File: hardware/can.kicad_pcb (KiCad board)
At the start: 2 copper layers, 45 x 35 mm, 33 parts, among them J1 DB9, P1 CON-SENSOR, P2 CONN_5, P3 CONN_5, U1 M24C64, U2 SC16IS740, U3 SP3232EBCN, U4 DRILL, U5 DRILL, U6 DRILL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

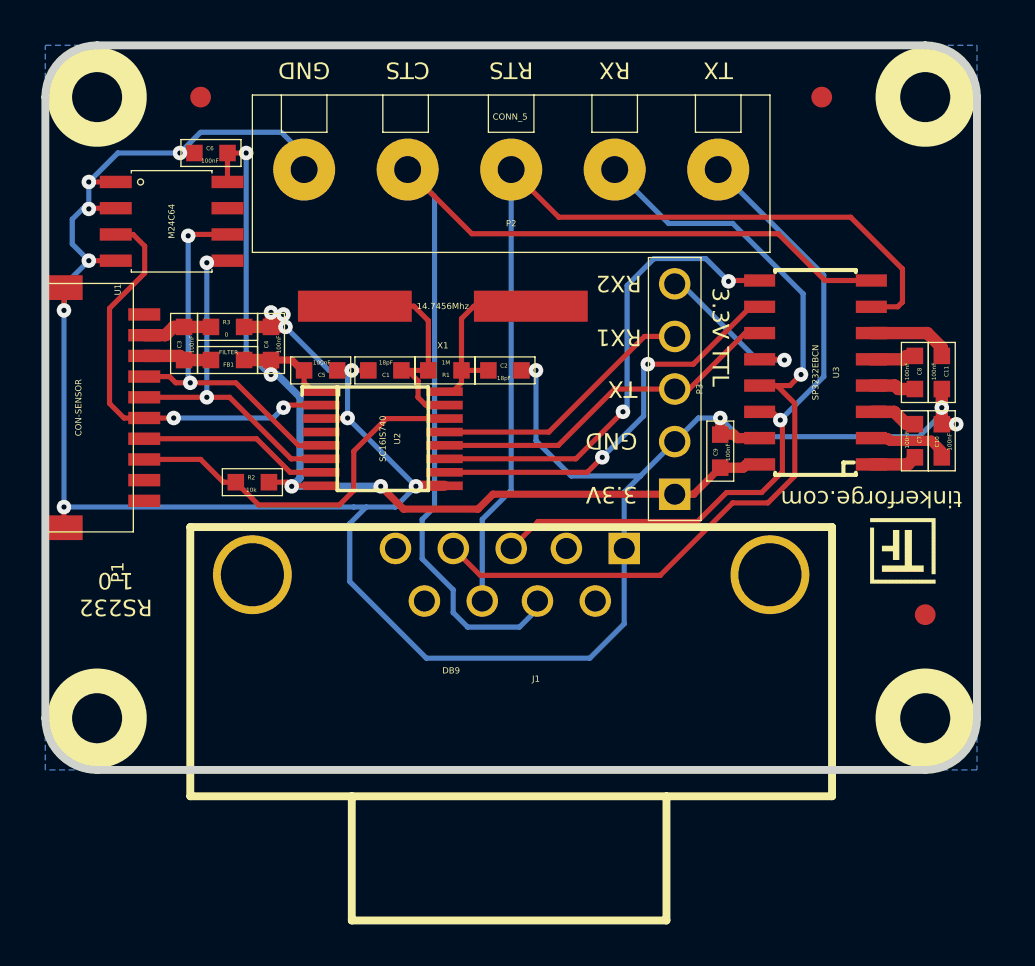
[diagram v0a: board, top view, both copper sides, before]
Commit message: fully routed
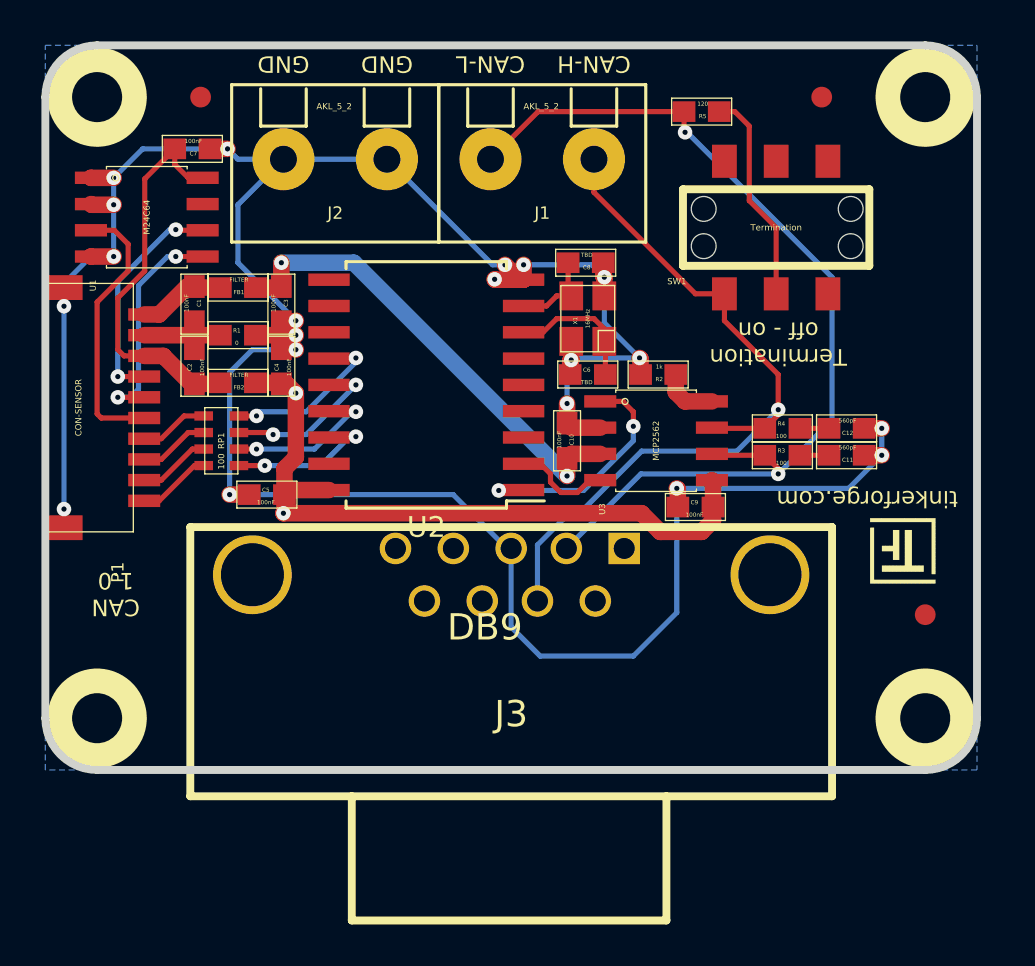
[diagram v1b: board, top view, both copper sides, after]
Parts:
- removed P2: CONN_5, AKL_5_5
- removed P3: CONN_5, pin_array_5x1
- added C12: 560pF, kicad-libraries:0603E, F.Cu at (164.0, 101.6)
- added FB2: FILTER, kicad-libraries:0603E, F.Cu at (134.6, 99.4)
- added J2: AKL_5_2, kicad-libraries:AKL_5_2, F.Cu at (139.3, 88.6)
- added J3: DB9, kicad-libraries:SUB09-EU, F.Cu at (147.8, 107.4)
- added R4: 100, kicad-libraries:0603E, F.Cu at (160.9, 101.6)
- added R5: 120, kicad-libraries:0603E, F.Cu at (157.0, 86.3)
- added RP1: 100, kicad-libraries:0603X4, F.Cu at (133.8, 102.2)
- added SW1: Termination, kicad-libraries:SLIDE_SWITCH, F.Cu at (160.6, 91.9)
- C1, C2: value 18pF -> 100nF; footprint 0603 -> kicad-libraries:0603E
- C10, C3, C4, C5, C7, C9, FB1: footprint 0603 -> kicad-libraries:0603E
- C11: value 100nF -> 560pF; footprint 0603 -> kicad-libraries:0603E
- C6, C8: value 100nF -> TBD; footprint 0603 -> kicad-libraries:0603E
- J1: value DB9 -> AKL_5_2; footprint SUB09-EU -> kicad-libraries:AKL_5_2
- P1: footprint CON-SENSOR -> kicad-libraries:CON-SENSOR
- R1: value 1M -> 0; footprint 0603 -> kicad-libraries:0603E
- R2: value 10k -> 1k; footprint 0603 -> kicad-libraries:0603E
- R3: value 0 -> 100; footprint 0603 -> kicad-libraries:0603E
- U1: footprint SOIC8 -> kicad-libraries:SOIC8
- U2: value SC16IS740 -> MCP2515; footprint TSSOP16 -> kicad-libraries:SOIC-18
- U3: value SP3232EBCN -> MCP2562; footprint SOIC16 -> kicad-libraries:SOIC8
- U4, U5, U6, U7: footprint DRILL_NP -> kicad-libraries:DRILL_NP
- X1: value 14.7456Mhz -> 16MHz; footprint HC49_US -> kicad-libraries:CRYSTAL_3225
- moved C7 37.6 mm to (132.4, 88.1), turned to 0 degrees
- moved R3 27.5 mm to (160.9, 102.9)
- moved C6 21.1 mm to (151.5, 99.0)
- moved R2 20.3 mm to (154.9, 99.0), turned to 0 degrees
- moved J1 18.9 mm to (149.3, 88.6), turned to 0 degrees
- moved C10 18.1 mm to (150.5, 102.2), turned to 90 degrees
- moved C8 16.8 mm to (151.4, 93.6), turned to 0 degrees
- moved C2 15.0 mm to (132.5, 98.6), turned to 270 degrees
- moved R1 10.1 mm to (134.6, 97.1), turned to 180 degrees
- moved C1 9.74 mm to (132.5, 95.6), turned to 90 degrees
- moved U3 8.38 mm to (154.8, 102.2), turned to 270 degrees
- moved X1 7.03 mm to (151.5, 96.3), turned to 90 degrees
- moved C5 6.54 mm to (136.0, 104.8), turned to 180 degrees
- moved C11 6.10 mm to (164.0, 102.9), turned to 0 degrees
- moved C3 5.07 mm to (136.7, 95.6), turned to 90 degrees
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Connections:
- C1 pad 1: GND -> Net-(C1-Pad1)
- C10 pad 1: GND -> +5V
- C10 pad 2: Net-(C10-Pad2) -> GND
- C11 pad 1: GND -> Net-(C11-Pad1)
- C11 pad 2: Net-(C11-Pad2) -> GND
- C2 pad 1: GND -> Net-(C1-Pad1)
- C2 pad 2: Net-(C2-Pad2) -> 3V3
- C3 pad 1: Net-(C3-Pad1) -> GND
- C3 pad 2: Net-(C3-Pad2) -> +5V
- C6 pad 1: VCC -> Net-(C6-Pad1)
- C7 pad 1: Net-(C7-Pad1) -> 3V3
- C7 pad 2: Net-(C7-Pad2) -> GND
- C8 pad 2: Net-(C8-Pad2) -> GND
- C9 pad 1: GND -> VCC
- C9 pad 2: VCC -> GND
- FB1 pad 1: Net-(C3-Pad2) -> Net-(C1-Pad2)
- FB1 pad 2: VCC -> +5V
- J1 pad 1: GND -> Net-(J1-Pad1)
- P1 pad 1: Net-(P1-Pad1) -> Net-(C1-Pad2)
- P1 pad 2: Net-(C3-Pad1) -> Net-(C1-Pad1)
- P1 pad 3: Net-(C3-Pad2) -> 3V3
- R1 pad 1: Net-(C1-Pad2) -> GND
- R1 pad 2: Net-(C2-Pad2) -> Net-(C1-Pad1)
- R2 pad 1: VCC -> GND
- R2 pad 2: Net-(P1-Pad8) -> Net-(R2-Pad2)
- R3 pad 1: GND -> Net-(C11-Pad1)
- R3 pad 2: Net-(C3-Pad1) -> Net-(J1-Pad1)
- U1 pad 7: Net-(U1-Pad7) -> (no net)
- U1 pad 8: VCC -> 3V3
- U2 pad 1: VCC -> Net-(U2-Pad1)
- U2 pad 10: Net-(U2-Pad10) -> (no net)
- U2 pad 11: Net-(U2-Pad11) -> (no net)
- U2 pad 12: Net-(P3-Pad3) -> (no net)
- U2 pad 14: Net-(P1-Pad8) -> Net-(RP1-Pad3)
- U2 pad 15: Net-(C1-Pad2) -> Net-(RP1-Pad2)
- U2 pad 16: Net-(C2-Pad2) -> Net-(RP1-Pad1)
- U2 pad 2: Net-(P1-Pad6) -> Net-(U2-Pad2)
- U2 pad 3: GND -> (no net)
- U2 pad 4: Net-(U2-Pad4) -> (no net)
- U2 pad 5: SCL -> (no net)
- U2 pad 6: SDA -> (no net)
- U2 pad 7: Net-(P1-Pad7) -> Net-(C6-Pad1)
- U2 pad 8: VCC -> Net-(C8-Pad1)
- U3 pad 1: Net-(C7-Pad1) -> Net-(U2-Pad1)
- U3 pad 2: Net-(C10-Pad2) -> GND
- U3 pad 3: Net-(C7-Pad2) -> +5V
- U3 pad 4: Net-(C8-Pad1) -> Net-(U2-Pad2)
- U3 pad 5: Net-(C8-Pad2) -> VCC
- U3 pad 6: Net-(C11-Pad2) -> Net-(J1-Pad1)
- U3 pad 7: Net-(J1-Pad8) -> Net-(J1-Pad2)
- U3 pad 8: Net-(J1-Pad7) -> Net-(R2-Pad2)
- X1 pad 1: Net-(C2-Pad2) -> Net-(C6-Pad1)
- X1 pad 2: Net-(C1-Pad2) -> Net-(C8-Pad1)
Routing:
- net Net-(J1-Pad7): track 52.5 -> 0.00 mm
- net Net-(J1-Pad1): track 0.00 -> 47.4 mm, vias 0 -> 2
- net Net-(J1-Pad8): track 45.5 -> 0.00 mm
- net Net-(J1-Pad4): track 42.3 -> 0.00 mm, vias 1 -> 0
- net Net-(J1-Pad2): track 0.00 -> 37.4 mm, vias 0 -> 1
- net Net-(J1-Pad3): track 34.0 -> 0.00 mm, vias 1 -> 0
- net Net-(U2-Pad11): track 23.2 -> 0.00 mm, vias 2 -> 0
- net +5V: track 0.00 -> 23.0 mm, vias 0 -> 2
- net Net-(U2-Pad10): track 19.9 -> 0.00 mm, vias 2 -> 0
- net 3V3: track 0.00 -> 18.9 mm
- net VCC: track 51.9 -> 33.8 mm, vias 4 -> 2
- net Net-(P3-Pad3): track 17.5 -> 0.00 mm
- net Net-(P1-Pad8): track 18.3 -> 3.41 mm
- net GND: track 131.3 -> 143.4 mm, vias 16 -> 20
- net Net-(U2-Pad1): track 0.00 -> 11.9 mm, vias 0 -> 2
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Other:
- board text added: "CAN 1.0"
- board text added: "CAN-H"
- board text added: "CAN-L"
- board text added: "Termination off - on"
- board text removed: "3.3V"
- board text removed: "3.3V TTL"
- board text removed: "CTS"
- board text removed: "RS232 1.0"
- board text removed: "RTS"
- board text removed: "RX"
- board text removed: "RX1"
- board text removed: "RX2"
- board text removed: "TX"
